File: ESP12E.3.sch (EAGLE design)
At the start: 24 parts, among them SW1 PTS840-GP-SMTR-LFS, U1 SPX3819M5-L-3-3

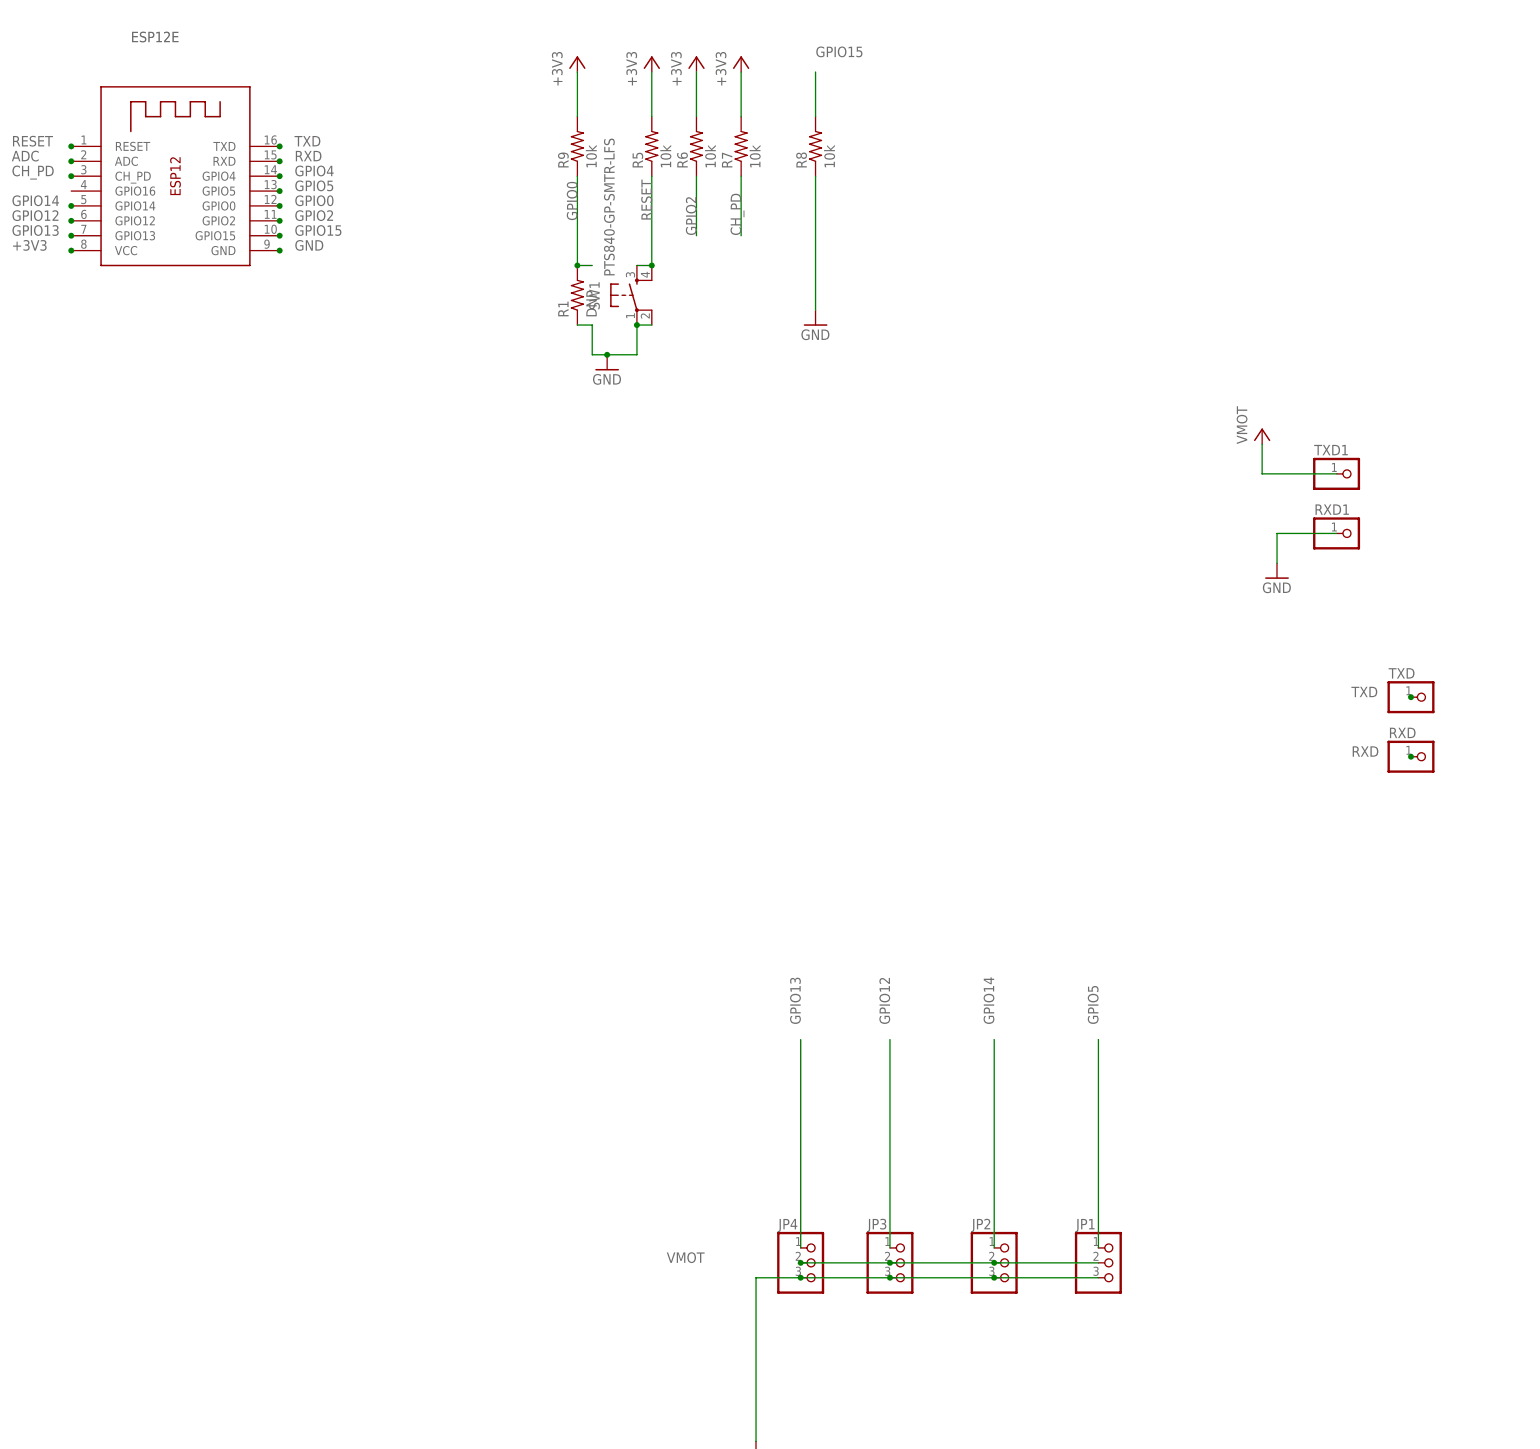
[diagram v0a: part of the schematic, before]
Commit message: New Programming Header
Modified loading method with 6 pin header.
Flipped board in layout as most parts were on bottom layer.
Board power now matches 3 pin servo cable.
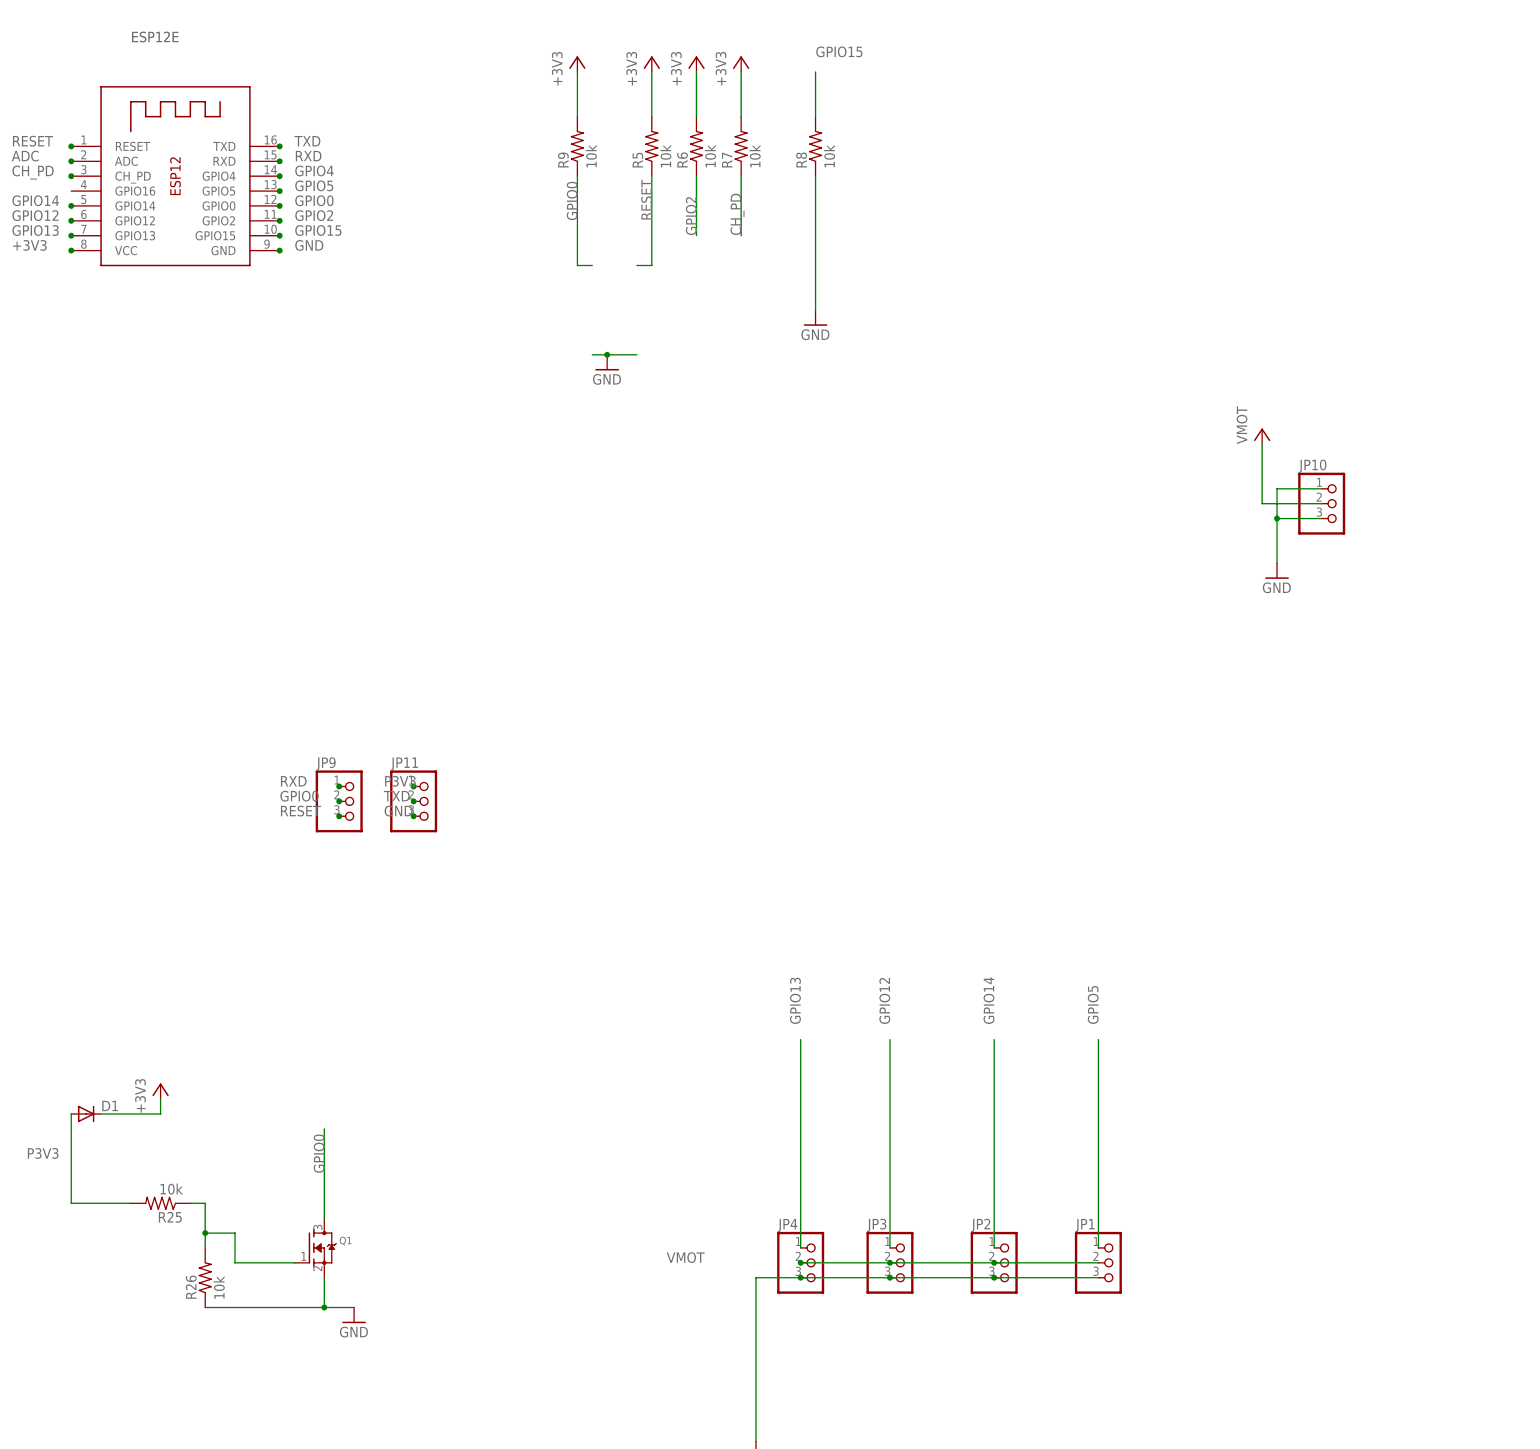
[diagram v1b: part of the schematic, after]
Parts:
- removed R1: DNP, adafruit:R-US_R0603
- removed RXD, RXD1, TXD, TXD1: (no value), adafruit:PINHD-1X1
- removed SW1: PTS840-GP-SMTR-LFS, PTS840-G_P-SMTR-LFS:PTS840-GP-SMTR-LFS
- added D1: (no value), diode:DIODE-DO214AC
- added JP10, JP11, JP9: (no value), adafruit:PINHD-1X3
- added Q1: (no value), adafruit:MOSFET-NREFLOW
- added R25, R26: 10k, adafruit:R-US_R0603
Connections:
- new net N$7: Q1.G, R25.1, R26.2
- new net P3V3: D1.A, JP11.1, R25.2
- net +3V3: now also D1.C
- net GND: now also JP10.1, JP10.3, JP11.3, Q1.S, R26.1; no longer R1.1, RXD1.1, SW1.P, SW1.P1
- net GPIO0: now also JP9.2, Q1.D; no longer R1.2
- net RESET: now also JP9.3; no longer SW1.S, SW1.S1
- net RXD: now also JP9.1; no longer RXD.1
- net TXD: now also JP11.2; no longer TXD.1
- net VMOT: now also JP10.2; no longer TXD1.1
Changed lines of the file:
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@@
 <part name="GND7" library="supply1" deviceset="GND" device=""/>
 <part name="GND8" library="supply1" deviceset="GND" device=""/>
-<part name="SW1" library="PTS840-G_P-SMTR-LFS" deviceset="PTS840-G*P-SMTR-LFS" device=""/>
-<part name="RXD" library="adafruit" deviceset="PINHD-1X1" device=""/>
-<part name="TXD" library="adafruit" deviceset="PINHD-1X1" device=""/>
 <part name="U1" library="SPX3819M5-L-3-3" deviceset="SPX3819M5-L-3-3" device=""/>
 <part name="+3V5" library="supply1" deviceset="+3V3" device=""/>
@@
 <part name="GND1" library="supply1" deviceset="GND" device=""/>
 <part name="C3" library="rcl" deviceset="CPOL-US" device="E2-4" value="DNP"/>
-<part name="R1" library="adafruit" deviceset="R-US_" device="R0603" value="DNP"/>
-<part name="TXD1" library="adafruit" deviceset="PINHD-1X1" device=""/>
-<part name="RXD1" library="adafruit" deviceset="PINHD-1X1" device=""/>
 <part name="GND2" library="supply1" deviceset="GND" device=""/>
 <part name="VMOT1" library="supply1" deviceset="VCC" device="" value="VMOT"/>
+<part name="JP10" library="adafruit" deviceset="PINHD-1X3" device=""/>
+<part name="GND13" library="supply1" deviceset="GND" device=""/>
+<part name="D1" library="diode" deviceset="DIODE-" device="DO214AC"/>
+<part name="Q1" library="adafruit" deviceset="MOSFET-N" device="REFLOW"/>
+<part name="R25" library="adafruit" deviceset="R-US_" device="R0603" value="10k"/>
+<part name="R26" library="adafruit" deviceset="R-US_" device="R0603" value="10k"/>
+<part name="+3V11" library="supply1" deviceset="+3V3" device=""/>
+<part name="JP9" library="adafruit" deviceset="PINHD-1X3" device=""/>
+<part name="JP11" library="adafruit" deviceset="PINHD-1X3" device=""/>
 </parts>
 <sheets>
@@
 <instance part="GND7" gate="1" x="149.86" y="198.12"/>
 <instance part="GND8" gate="1" x="185.42" y="205.74"/>
-<instance part="SW1" gate="1" x="154.94" y="210.82"/>
-<instance part="RXD" gate="G$1" x="289.56" y="132.08"/>
-<instance part="TXD" gate="G$1" x="289.56" y="142.24"/>
 <instance part="U1" gate="A" x="368.3" y="236.22"/>
 <instance part="+3V5" gate="G$1" x="398.78" y="246.38"/>
@@
 <instance part="GND1" gate="1" x="175.26" y="12.7"/>
 <instance part="C3" gate="G$1" x="358.14" y="177.8"/>
-<instance part="R1" gate="G$1" x="144.78" y="210.82" rot="R90"/>
-<instance part="TXD1" gate="G$1" x="276.86" y="180.34"/>
-<instance part="RXD1" gate="G$1" x="276.86" y="170.18"/>
 <instance part="GND2" gate="1" x="264.16" y="162.56"/>
 <instance part="VMOT1" gate="VCC" x="261.62" y="187.96"/>
+<instance part="JP10" gate="A" x="274.32" y="175.26"/>
+<instance part="GND13" gate="1" x="106.68" y="35.56"/>
+<instance part="D1" gate="G$1" x="60.96" y="71.12"/>
+<instance part="Q1" gate="G$1" x="99.06" y="48.26"/>
+<instance part="R25" gate="G$1" x="73.66" y="55.88" rot="R180"/>
+<instance part="R26" gate="G$1" x="81.28" y="43.18" rot="R90"/>
+<instance part="+3V11" gate="G$1" x="73.66" y="76.2"/>
+<instance part="JP9" gate="A" x="106.68" y="124.46"/>
+<instance part="JP11" gate="A" x="119.38" y="124.46"/>
 </instances>
 <busses>
@@
 </segment>
 <segment>
-<wire x1="144.78" y1="205.74" x2="147.32" y2="205.74" width="0.1524" layer="91"/>
-<wire x1="147.32" y1="205.74" x2="147.32" y2="200.66" width="0.1524" layer="91"/>
 <pinref part="GND7" gate="1" pin="GND"/>
 <wire x1="147.32" y1="200.66" x2="149.86" y2="200.66" width="0.1524" layer="91"/>
 <wire x1="149.86" y1="200.66" x2="154.94" y2="200.66" width="0.1524" layer="91"/>
 <junction x="149.86" y="200.66"/>
-<pinref part="SW1" gate="1" pin="P1"/>
-<pinref part="SW1" gate="1" pin="P"/>
-<wire x1="157.48" y1="205.74" x2="154.94" y2="205.74" width="0.1524" layer="91"/>
-<wire x1="154.94" y1="200.66" x2="154.94" y2="205.74" width="0.1524" layer="91"/>
-<junction x="154.94" y="205.74"/>
-<pinref part="R1" gate="G$1" pin="1"/>
 </segment>
 <segment>
@@
 </segment>
 <segment>
-<pinref part="RXD1" gate="G$1" pin="1"/>
 <pinref part="GND2" gate="1" pin="GND"/>
-<wire x1="274.32" y1="170.18" x2="264.16" y2="170.18" width="0.1524" layer="91"/>
-<wire x1="264.16" y1="170.18" x2="264.16" y2="165.1" width="0.1524" layer="91"/>
+<wire x1="264.16" y1="172.72" x2="264.16" y2="165.1" width="0.1524" layer="91"/>
+<pinref part="JP10" gate="A" pin="3"/>
+<wire x1="271.78" y1="172.72" x2="264.16" y2="172.72" width="0.1524" layer="91"/>
+<pinref part="JP10" gate="A" pin="1"/>
+<wire x1="271.78" y1="177.8" x2="264.16" y2="177.8" width="0.1524" layer="91"/>
+<wire x1="264.16" y1="177.8" x2="264.16" y2="172.72" width="0.1524" layer="91"/>
+<junction x="264.16" y="172.72"/>
+</segment>
+<segment>
+<pinref part="GND13" gate="1" pin="GND"/>
+<pinref part="Q1" gate="G$1" pin="S"/>
+<wire x1="101.6" y1="43.18" x2="101.6" y2="38.1" width="0.1524" layer="91"/>
+<wire x1="101.6" y1="38.1" x2="106.68" y2="38.1" width="0.1524" layer="91"/>
+<pinref part="R26" gate="G$1" pin="1"/>
+<wire x1="101.6" y1="38.1" x2="81.28" y2="38.1" width="0.1524" layer="91"/>
+<junction x="101.6" y="38.1"/>
+</segment>
+<segment>
+<pinref part="JP11" gate="A" pin="3"/>
+<junction x="116.84" y="121.92"/>
+<label x="111.76" y="121.92" size="1.778" layer="95"/>
 </segment>
 </net>
@@
 </segment>
 <segment>
-<pinref part="TXD1" gate="G$1" pin="1"/>
 <pinref part="VMOT1" gate="VCC" pin="VCC"/>
-<wire x1="274.32" y1="180.34" x2="261.62" y2="180.34" width="0.1524" layer="91"/>
-<wire x1="261.62" y1="180.34" x2="261.62" y2="185.42" width="0.1524" layer="91"/>
+<pinref part="JP10" gate="A" pin="2"/>
+<wire x1="271.78" y1="175.26" x2="261.62" y2="175.26" width="0.1524" layer="91"/>
+<wire x1="261.62" y1="175.26" x2="261.62" y2="185.42" width="0.1524" layer="91"/>
 </segment>
 </net>
@@
 <junction x="391.16" y="238.76"/>
 </segment>
+<segment>
+<pinref part="D1" gate="G$1" pin="C"/>
+<pinref part="+3V11" gate="G$1" pin="+3V3"/>
+<wire x1="63.5" y1="71.12" x2="73.66" y2="71.12" width="0.1524" layer="91"/>
+<wire x1="73.66" y1="71.12" x2="73.66" y2="73.66" width="0.1524" layer="91"/>
+</segment>
 </net>
 <net name="GPIO15" class="0">
@@
 </segment>
 <segment>
-<pinref part="SW1" gate="1" pin="S"/>
-<pinref part="SW1" gate="1" pin="S1"/>
 <wire x1="154.94" y1="215.9" x2="157.48" y2="215.9" width="0.1524" layer="91"/>
 <pinref part="R5" gate="G$1" pin="1"/>
 <wire x1="157.48" y1="215.9" x2="157.48" y2="231.14" width="0.1524" layer="91"/>
-<junction x="157.48" y="215.9"/>
 <label x="157.48" y="223.52" size="1.778" layer="95" rot="R90"/>
+</segment>
+<segment>
+<pinref part="JP9" gate="A" pin="3"/>
+<junction x="104.14" y="121.92"/>
+<label x="93.98" y="121.92" size="1.778" layer="95"/>
 </segment>
 </net>
@@
 <net name="RXD" class="0">
 <segment>
-<pinref part="RXD" gate="G$1" pin="1"/>
-<junction x="287.02" y="132.08"/>
-<label x="276.86" y="132.08" size="1.778" layer="95"/>
-</segment>
-<segment>
 <pinref part="X1" gate="G$1" pin="RXD"/>
 <junction x="93.98" y="233.68"/>
 <label x="96.52" y="233.68" size="1.778" layer="95"/>
 </segment>
+<segment>
+<pinref part="JP9" gate="A" pin="1"/>
+<junction x="104.14" y="127"/>
+<label x="93.98" y="127" size="1.778" layer="95"/>
+</segment>
 </net>
 <net name="TXD" class="0">
-<segment>
-<pinref part="TXD" gate="G$1" pin="1"/>
-<junction x="287.02" y="142.24"/>
-<label x="276.86" y="142.24" size="1.778" layer="95"/>
-</segment>
 <segment>
 <pinref part="X1" gate="G$1" pin="TXD"/>
 <junction x="93.98" y="236.22"/>
 <label x="96.52" y="236.22" size="1.778" layer="95"/>
+</segment>
+<segment>
+<pinref part="JP11" gate="A" pin="2"/>
+<junction x="116.84" y="124.46"/>
+<label x="111.76" y="124.46" size="1.778" layer="95"/>
 </segment>
 </net>
@@
 <label x="144.78" y="223.52" size="1.778" layer="95" rot="R90"/>
 <pinref part="R9" gate="G$1" pin="1"/>
-<pinref part="R1" gate="G$1" pin="2"/>
-<junction x="144.78" y="215.9"/>
+</segment>
+<segment>
+<wire x1="101.6" y1="68.58" x2="101.6" y2="53.34" width="0.1524" layer="91"/>
+<label x="101.6" y="60.96" size="1.778" layer="95" rot="R90"/>
+<pinref part="Q1" gate="G$1" pin="D"/>
+</segment>
+<segment>
+<pinref part="JP9" gate="A" pin="2"/>
+<junction x="104.14" y="124.46"/>
+<label x="93.98" y="124.46" size="1.778" layer="95"/>
 </segment>
 </net>
@@
 </segment>
 </net>
+<net name="N$7" class="0">
+<segment>
+<pinref part="Q1" gate="G$1" pin="G"/>
+<wire x1="96.52" y1="45.72" x2="86.36" y2="45.72" width="0.1524" layer="91"/>
+<wire x1="86.36" y1="45.72" x2="86.36" y2="50.8" width="0.1524" layer="91"/>
+<wire x1="86.36" y1="50.8" x2="81.28" y2="50.8" width="0.1524" layer="91"/>
+<pinref part="R26" gate="G$1" pin="2"/>
+<wire x1="81.28" y1="50.8" x2="81.28" y2="48.26" width="0.1524" layer="91"/>
+<pinref part="R25" gate="G$1" pin="1"/>
+<wire x1="78.74" y1="55.88" x2="81.28" y2="55.88" width="0.1524" layer="91"/>
+<wire x1="81.28" y1="55.88" x2="81.28" y2="50.8" width="0.1524" layer="91"/>
+<junction x="81.28" y="50.8"/>
+</segment>
+</net>
+<net name="P3V3" class="0">
+<segment>
+<pinref part="D1" gate="G$1" pin="A"/>
+<wire x1="58.42" y1="71.12" x2="58.42" y2="55.88" width="0.1524" layer="91"/>
+<pinref part="R25" gate="G$1" pin="2"/>
+<wire x1="58.42" y1="55.88" x2="68.58" y2="55.88" width="0.1524" layer="91"/>
+<label x="50.8" y="63.5" size="1.778" layer="95"/>
+</segment>
+<segment>
+<pinref part="JP11" gate="A" pin="1"/>
+<junction x="116.84" y="127"/>
+<label x="111.76" y="127" size="1.778" layer="95"/>
+</segment>
+</net>

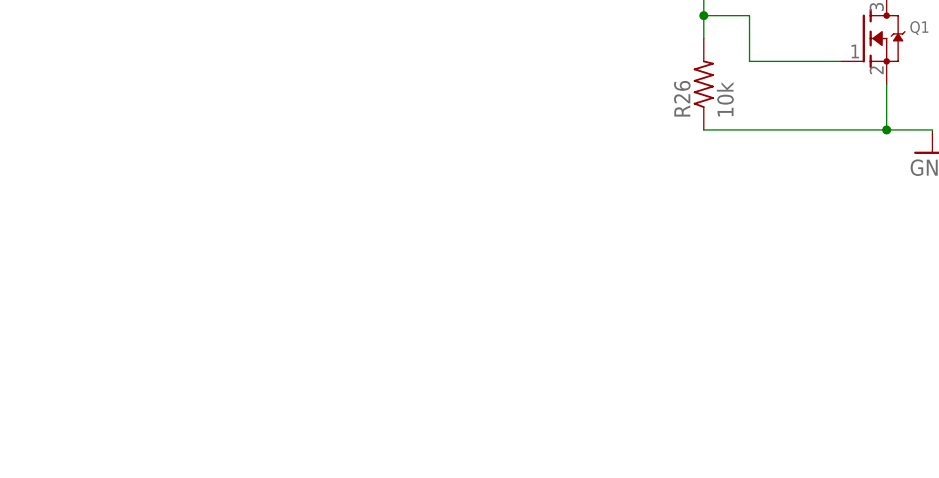
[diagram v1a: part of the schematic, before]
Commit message: License Update
Licensed under CERN OHL v.1.2 or later
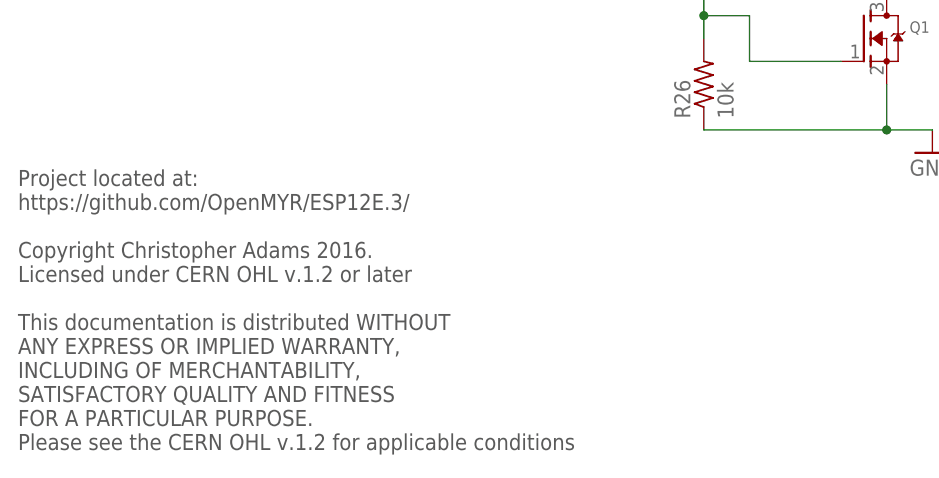
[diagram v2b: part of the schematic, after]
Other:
- note added: "Project located at: https://github.com/OpenMYR/ESP12E.3/ Copyright Christopher Adams 2016. Licensed under CERN OHL v.1.2 or later This documentation is distributed WITHOUT ANY EXPRESS OR IMPLIED WARRANTY, INCLUDING OF MERCHANTABILITY, SATISFACTORY QUALITY AND FITNESS FOR A PARTICULAR PURPOSE. Please see the CERN OHL v.1.2 for applicable conditions"
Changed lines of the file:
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@@
 <text x="353.06" y="256.54" size="1.778" layer="97">3.3 Volt Regulator</text>
 <text x="68.58" y="254" size="1.778" layer="97">ESP12E</text>
+<text x="5.08" y="2.54" size="1.778" layer="97">Project located at:
+https://github.com/OpenMYR/ESP12E.3/
+Copyright Christopher Adams 2016.
+Licensed under CERN OHL v.1.2 or later
+This documentation is distributed WITHOUT
+ANY EXPRESS OR IMPLIED WARRANTY,
+INCLUDING OF MERCHANTABILITY,
+SATISFACTORY QUALITY AND FITNESS
+FOR A PARTICULAR PURPOSE.
+Please see the CERN OHL v.1.2 for applicable conditions</text>
+<text x="5.08" y="7.62" size="1.778" layer="97"></text>
 </plain>
 <instances>
@@
 </schematic>
 </drawing>
+<compatibility>
+<note version="6.3" minversion="6.2.2" severity="warning">
+Since Version 6.2.2 text objects can contain more than one line,
+which will not be processed correctly with this version.
+</note>
+</compatibility>
 </eagle>
